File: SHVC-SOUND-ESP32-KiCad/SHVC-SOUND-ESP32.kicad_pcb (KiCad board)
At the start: 2 copper layers, 74.1 x 66.5 mm, 33 parts, among them J1 PJ-324M, J3 12V in (USB-PD), J4 SHVC-SOUND module, U1 ESP32 DevKit V1 (30pin), U2 74HCT541N (data write), U3 74HCT541N (control), U4 74LVC245N (data read, DIR=B->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, U6 TDA7053A, U7 M78AR05-0.5

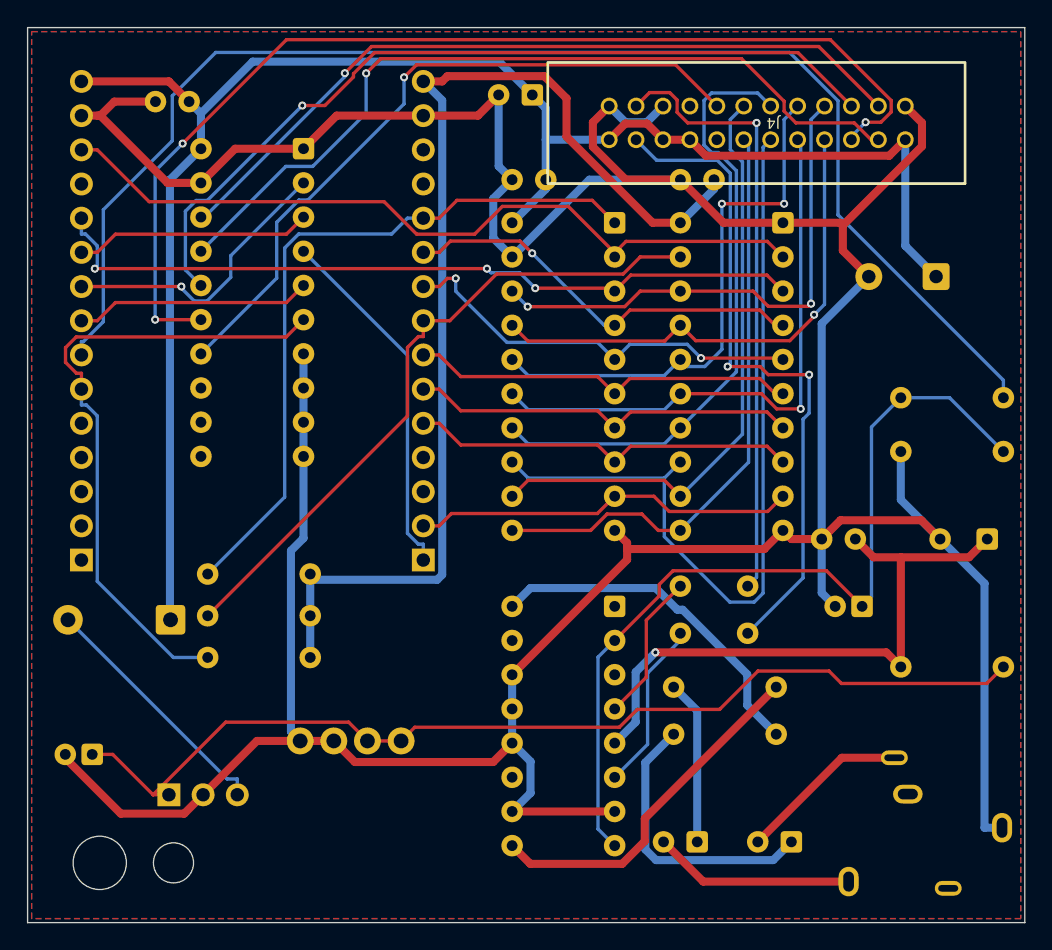
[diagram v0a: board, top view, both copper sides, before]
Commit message: ESP32版基板 r0.4: ライン出力・MUTE制御・表面ロゴシルク・GND強化
- ライン出力を追加: SHVC-SOUNDの音声 → 10µF無極性 → 47kで0V基準 → 100Ω → 端子台J5(L/GND/R)。
  アンプ(TDA7053A)とステレオジャックはそのまま
- MUTE制御: GPIO15 → 74HCT541N(U3)の空きチャンネル → SHVC-SOUND 20番。10kで引き下げ、起動中は消音
- 電源線を太く(5V系0.8mm、GND・12V・3.3V・アンプ出力0.6mm、音声0.4mm)
- GNDスティッチングビアを2mm格子で追加(表裏のGNDベタをつなぎ、島を減らす)。固定穴の周りは配線禁止
- 表面シルクにロゴ(art/logo.png → make_logo_grid.ps1 で0.1mmグリッド化)・Made by SHIMA・スペック表
- フェライトビーズFB1を10Ω(R10)に置き換え、固定穴をNPTH化

Co-Authored-By: Claude Opus 5 <noreply@anthropic.com>
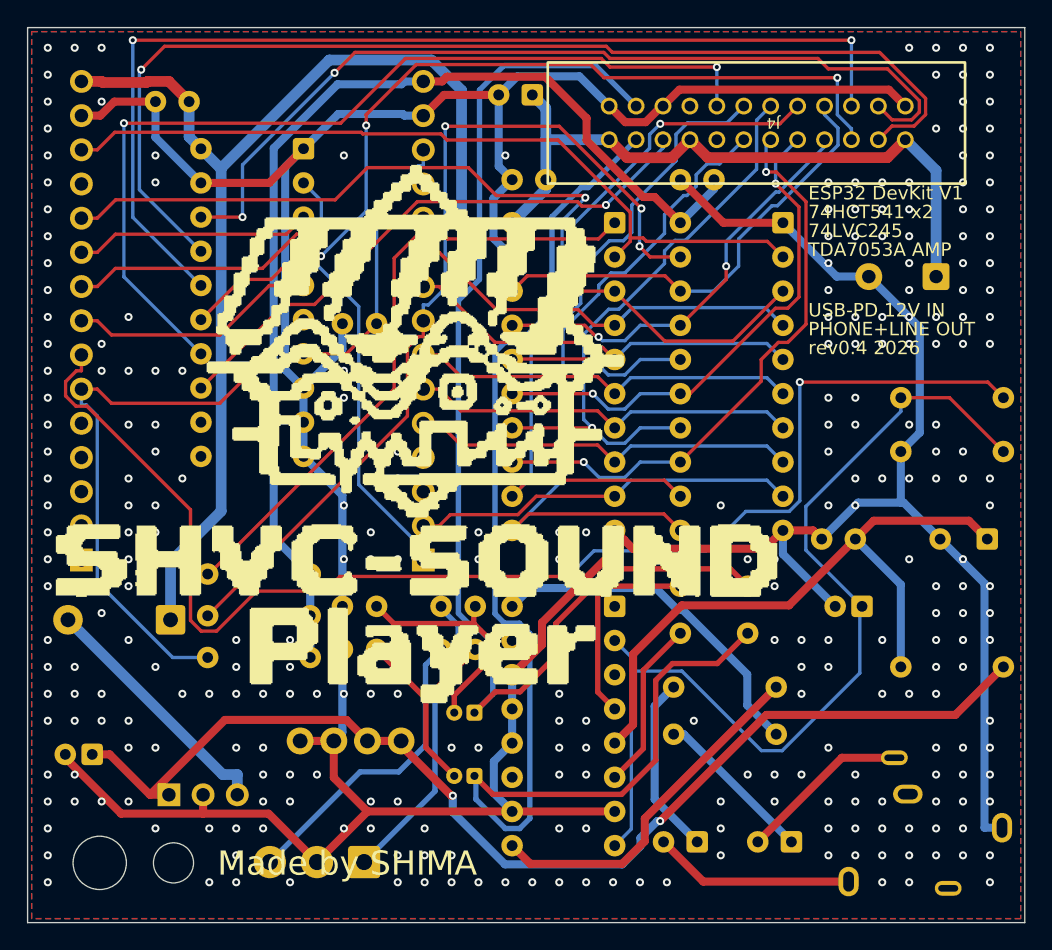
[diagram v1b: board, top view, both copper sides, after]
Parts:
- added C14: 10u NP, Capacitor_THT:CP_Radial_D4.0mm_P1.50mm, B.Cu at (133.2, 150.9)
- added C15: 10u NP, Capacitor_THT:CP_Radial_D4.0mm_P1.50mm, B.Cu at (133.2, 155.6)
- added J5: LINE OUT, TerminalBlock_Phoenix:TerminalBlock_Phoenix_PT-1,5-3-3.5-H_1x03_P3.50mm_Horizontal, B.Cu at (125.0, 162.0)
- added R11: 100, Resistor_THT:R_Axial_DIN0207_L6.3mm_D2.5mm_P2.54mm_Vertical, B.Cu at (133.3, 143.0)
- added R12: 100, Resistor_THT:R_Axial_DIN0207_L6.3mm_D2.5mm_P2.54mm_Vertical, B.Cu at (133.3, 146.2)
- added R13: 47k, Resistor_THT:R_Axial_DIN0207_L6.3mm_D2.5mm_P2.54mm_Vertical, B.Cu at (125.9, 143.0)
- added R14: 47k, Resistor_THT:R_Axial_DIN0207_L6.3mm_D2.5mm_P2.54mm_Vertical, B.Cu at (125.9, 146.2)
- added R15: 10k, Resistor_THT:R_Axial_DIN0207_L6.3mm_D2.5mm_P2.54mm_Vertical, B.Cu at (125.9, 122.0)
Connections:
- J4 pad 20: +5V -> SHVC_MUTE
- U1 pad 28: unconnected-(U1-IO15-Pad28) -> MUTE_3V3
- U3 pad 13: unconnected-(U3-Y6-Pad13) -> SHVC_MUTE
- U3 pad 7: GND -> MUTE_3V3
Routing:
- net AUDIO_R: track 49.9 -> 93.8 mm, vias 2 -> 0
- net AUDIO_L: track 45.5 -> 89.0 mm, vias 1 -> 0
- net SHVC_MUTE: track 0.00 -> 42.6 mm, vias 0 -> 1
- net LINE_R: track 0.00 -> 22.8 mm
- net LINE_L: track 0.00 -> 22.4 mm
- net MUTE_3V3: track 0.00 -> 20.9 mm
- net SHVC_A1: track 60.9 -> 81.5 mm
- net SHVC_D5: track 61.4 -> 43.5 mm, vias 0 -> 2
- net OE_R: track 49.8 -> 67.5 mm, vias 0 -> 3
- net LOUT_L: track 0.00 -> 17.5 mm
- net LOUT_R: track 0.00 -> 17.0 mm
- net SHVC_RESET: track 52.1 -> 68.7 mm, vias 1 -> 2
- net SHVC_WR: track 62.1 -> 78.6 mm, vias 1 -> 2
- net SHVC_RD: track 79.9 -> 64.8 mm
- net GND: track 299.8 -> 314.0 mm, vias 0 -> 290
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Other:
- board text added: "74HCT541 x2"
- board text added: "74LVC245"
- board text added: "ESP32 DevKit V1"
- board text added: "Made by SHIMA"
- board text added: "PHONE+LINE OUT"
- board text added: "SHVC-SOUND ESP32 r0.4"
- board text added: "TDA7053A AMP"
- board text added: "USB-PD 12V IN"
- board text added: "rev0.4 2026"
- board text removed: "SHVC-SOUND ESP32 r0.3"
